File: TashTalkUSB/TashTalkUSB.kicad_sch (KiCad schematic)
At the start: 32 parts, among them J1 TC2030, J3 USB_C_Receptacle_USB2.0_14P, U1 CP2102N-Axx-xQFN20, U2 PIC12F1840-xSN, U3 SN65HVD1473DGSR

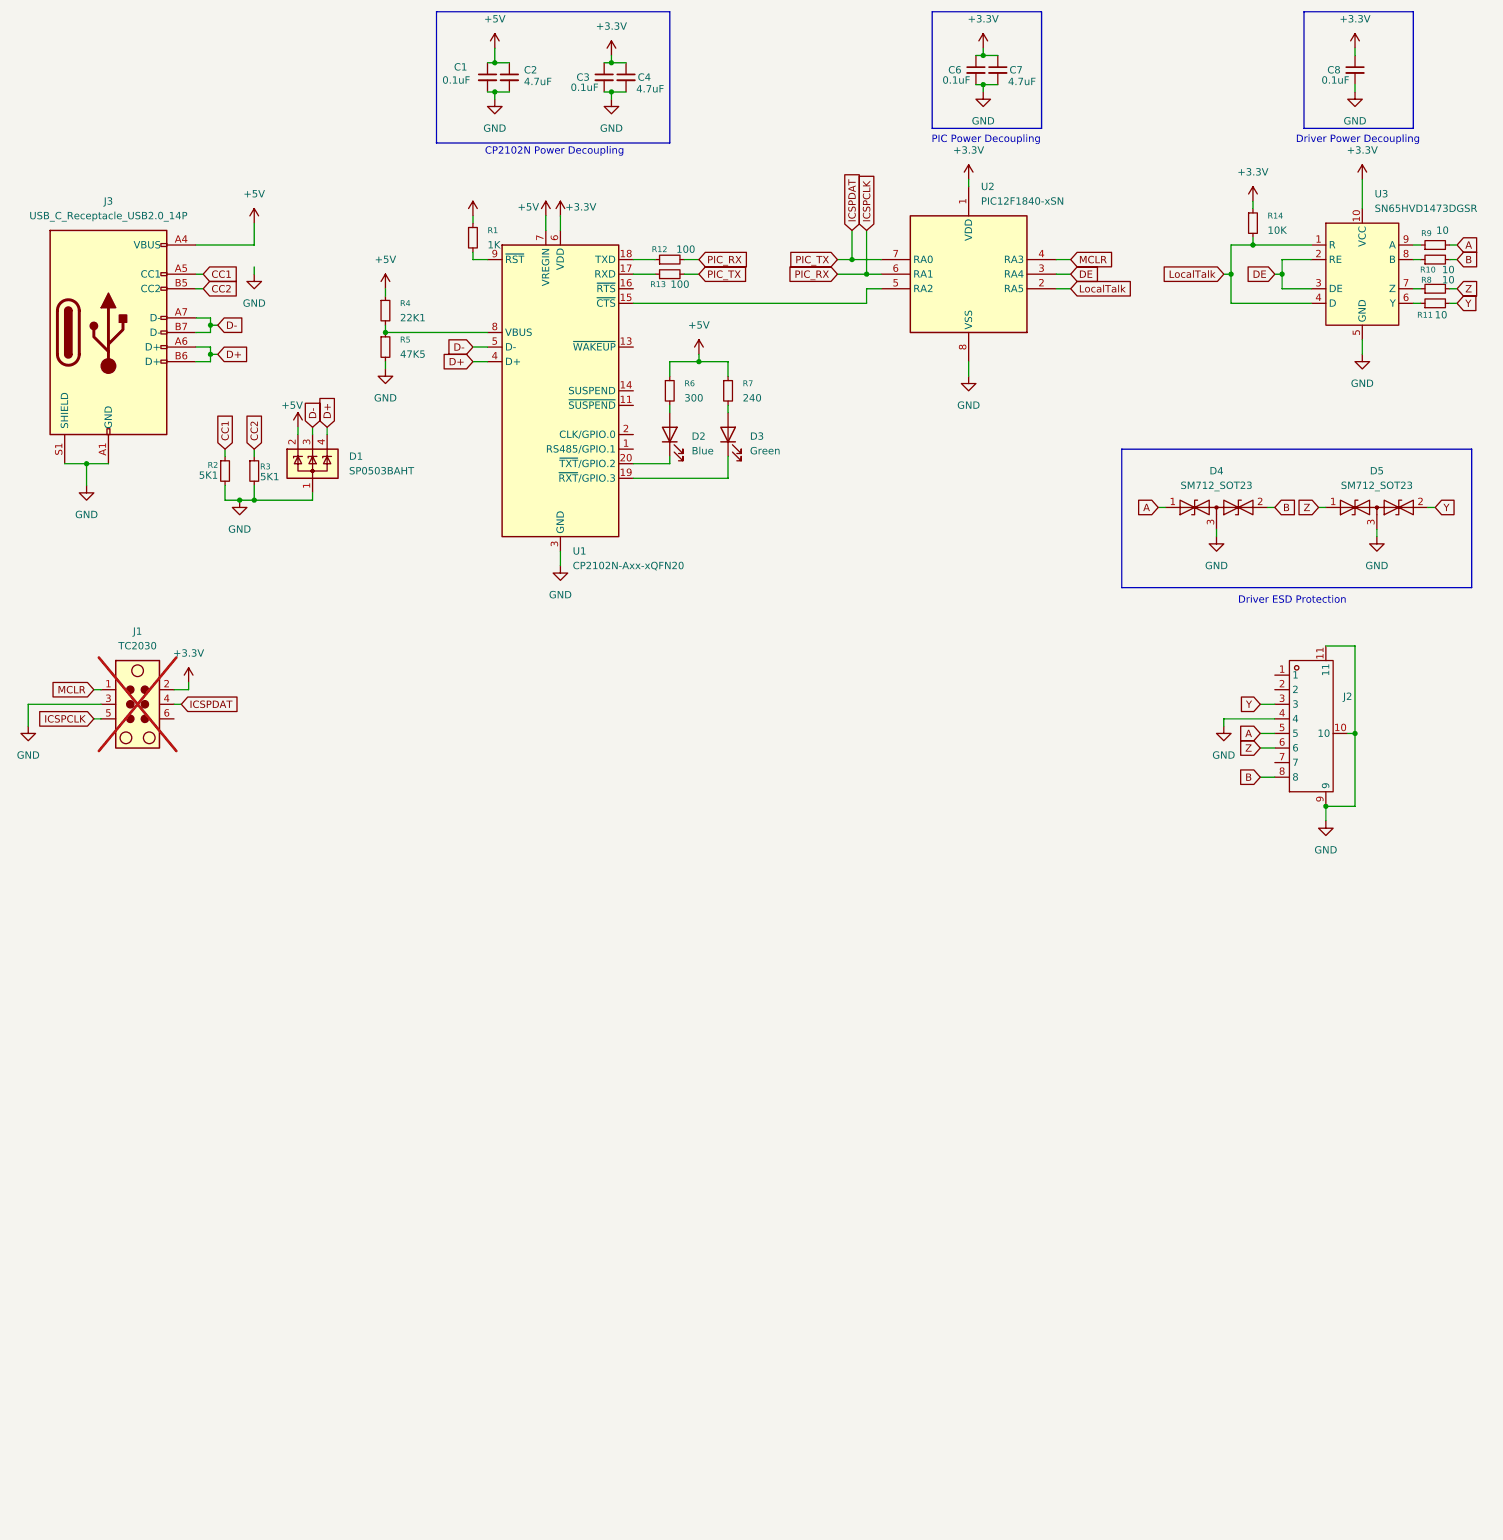
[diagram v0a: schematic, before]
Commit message: Update PCB and schematic with fixed mini-DIN 8 pinout
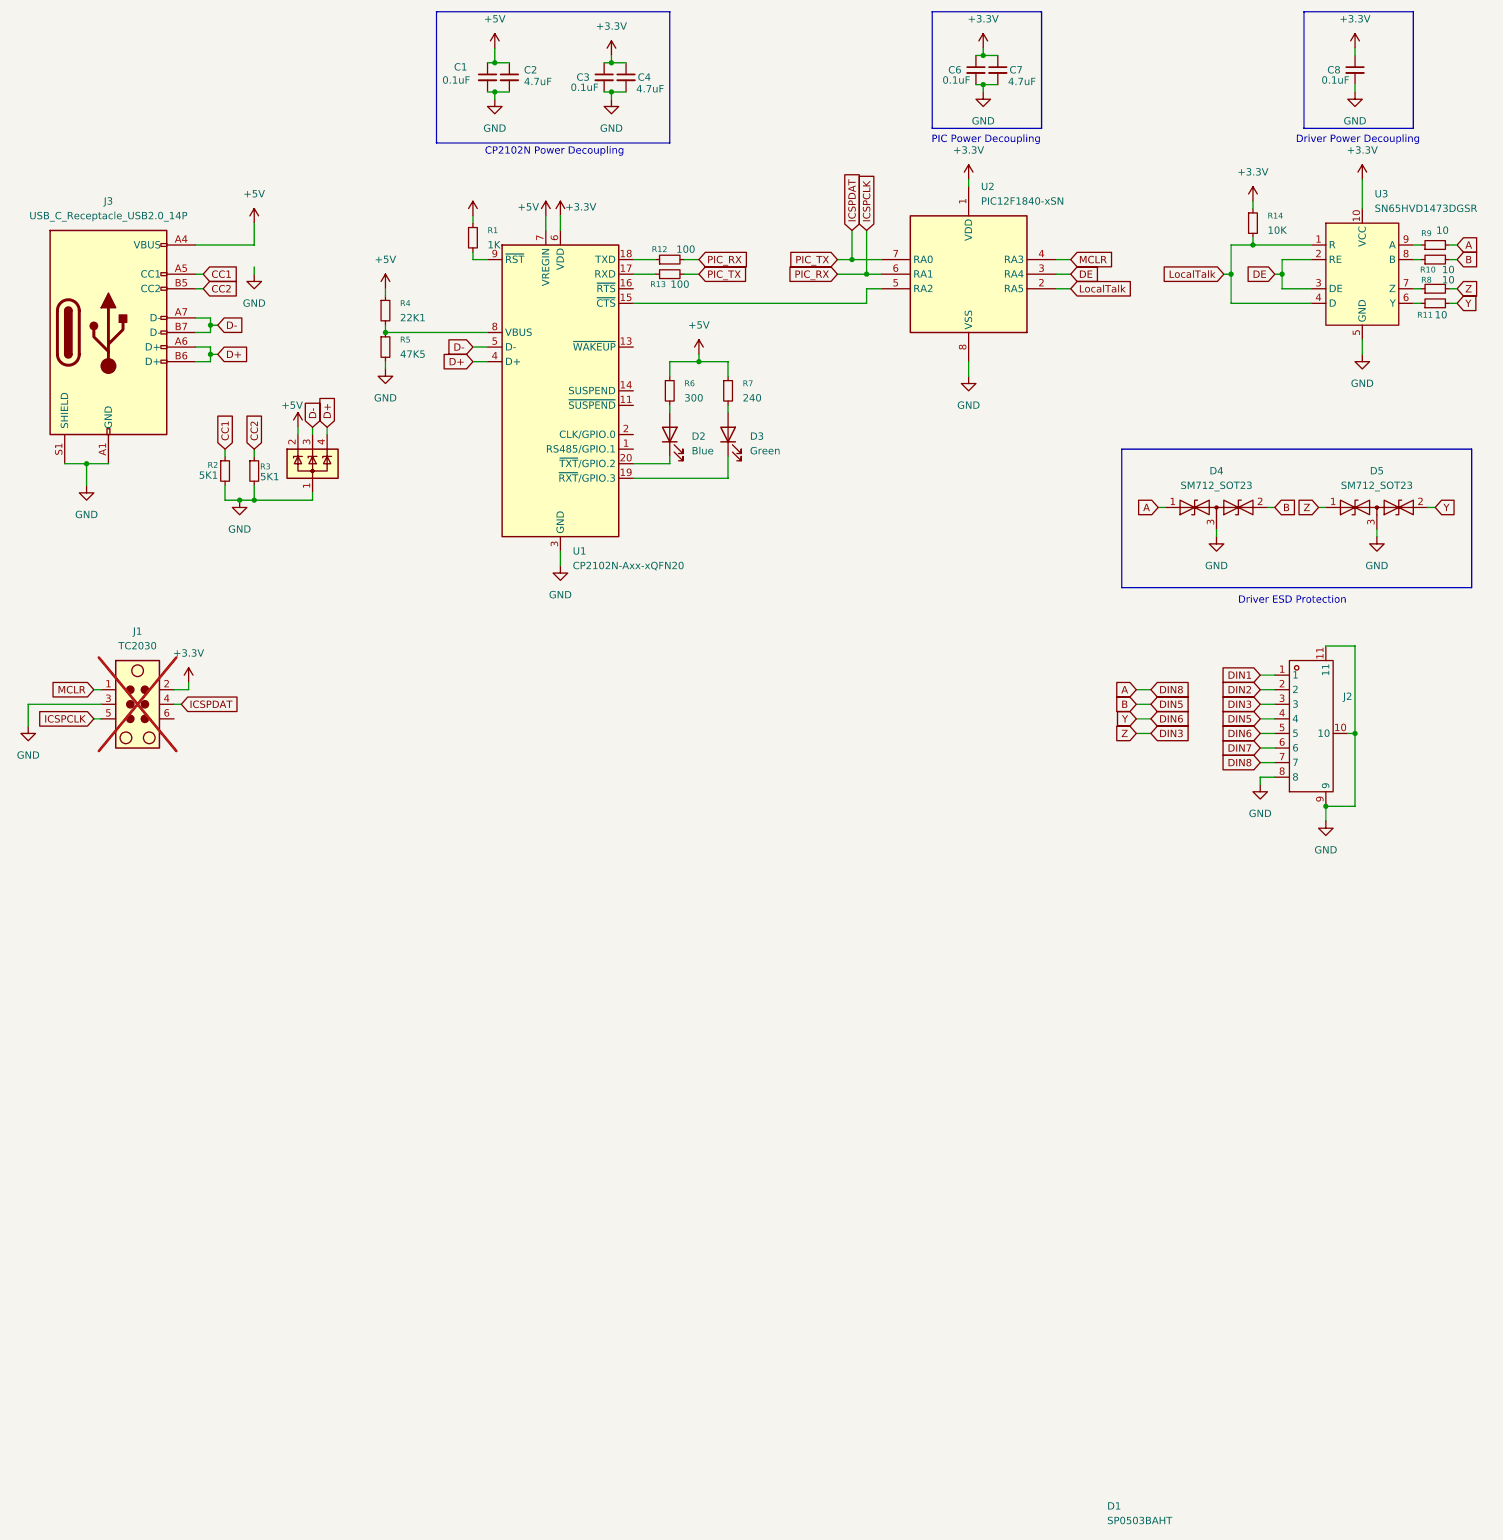
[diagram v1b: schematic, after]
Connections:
- net A: now also J2.7; no longer J2.5
- net B: now also J2.4; no longer J2.8
- net GND: now also J2.8; no longer J2.4
- net DIN1: now reaches J2.1
- net DIN2: now reaches J2.2
- net Y renamed DIN6
- net DIN6: now also J2.5; no longer J2.3
- net Z renamed DIN3
- net DIN3: now also J2.3; no longer J2.6
- new net DIN7: J2.6

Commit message: TashTalk USB Rev 2
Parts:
- C1, C3, C6, C8: LCSC C1591 -> C14663
- R1: LCSC C22548 -> C21190
- R10, R11, R8, R9: LCSC C2906983 -> C22859
- R12, R13: LCSC C2906981 -> C22775
- R14: LCSC C2930027 -> C25804
- R2, R3: LCSC C2907044 -> C23186
- R4: LCSC C2960862 -> C31850
- R5: LCSC C2933225 -> C25819
- R6: LCSC C2930092 -> C23025
- R7: LCSC C2907130 -> C23350
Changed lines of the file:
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@@
 			)
 		)
-		(property "LCSC" "C2907044"
+		(property "LCSC" "C23186 "
 			(at 55.88 92.71 0)
 			(effects
@@
 			)
 		)
-		(property "LCSC" "C2906981"
+		(property "LCSC" "C22775 "
 			(at 128.27 58.42 90)
 			(effects
@@
 			)
 		)
-		(property "LCSC" "C1591"
+		(property "LCSC" "C14663"
 			(at 247.65 22.86 0)
 			(effects
@@
 			)
 		)
-		(property "LCSC" "C2933225"
+		(property "LCSC" "C25819 "
 			(at 78.74 71.12 0)
 			(effects
@@
 			)
 		)
-		(property "LCSC" "C2960862"
+		(property "LCSC" "C31850"
 			(at 78.74 64.77 0)
 			(effects
@@
 			)
 		)
-		(property "LCSC" "C1591"
+		(property "LCSC" "C14663"
 			(at 116.84 24.13 0)
 			(effects
@@
 			)
 		)
-		(property "LCSC" "C2906983"
+		(property "LCSC" "C22859 "
 			(at 261.62 60.96 90)
 			(effects
@@
 			)
 		)
-		(property "LCSC" "C2930092"
+		(property "LCSC" "C23025 "
 			(at 128.27 78.74 0)
 			(effects
@@
 			)
 		)
-		(property "LCSC" "C2930027"
+		(property "LCSC" "C25804 "
 			(at 229.87 49.53 0)
 			(effects
@@
 			)
 		)
-		(property "LCSC" "C2906981"
+		(property "LCSC" "C22775 "
 			(at 128.27 55.88 90)
 			(effects
@@
 			)
 		)
-		(property "LCSC" "C2906983"
+		(property "LCSC" "C22859 "
 			(at 261.62 53.34 90)
 			(effects
@@
 			)
 		)
-		(property "LCSC" "C2906983"
+		(property "LCSC" "C22859 "
 			(at 261.62 55.88 90)
 			(effects
@@
 			)
 		)
-		(property "LCSC" "C1591"
+		(property "LCSC" "C14663"
 			(at 181.61 22.86 0)
 			(effects
@@
 			)
 		)
-		(property "LCSC" "C2906983"
+		(property "LCSC" "C22859 "
 			(at 261.62 63.5 90)
 			(effects
@@
 			)
 		)
-		(property "LCSC" "C22548"
+		(property "LCSC" "C21190 "
 			(at 93.98 52.07 0)
 			(effects
@@
 			)
 		)
-		(property "LCSC" "C2907130"
+		(property "LCSC" "C23350"
 			(at 138.43 78.74 0)
 			(effects
@@
 			)
 		)
-		(property "LCSC" "C2907044"
+		(property "LCSC" "C23186 "
 			(at 50.8 92.71 0)
 			(effects
@@
 			)
 		)
-		(property "LCSC" "C1591"
+		(property "LCSC" "C14663"
 			(at 96.52 24.13 0)
 			(effects
